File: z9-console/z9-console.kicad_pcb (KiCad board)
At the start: 2 copper layers, 89.5 x 55.5 mm, 130 parts, among them J10 Screw_Terminal_01x06, J2 LCD 3.2" 240x320 Conn_01x14_P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, J4 Conn_01x04_Pin, J6 ST_STDC14 - SAMTEC_FTSH-107-0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, J7 TC2070 - TAG Connect, J801 USB_C_Receptacle_USB2.0_16P, J9 JST GH, Q701 AO3400A, SW2 SW_Push, SW3 SW_Push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

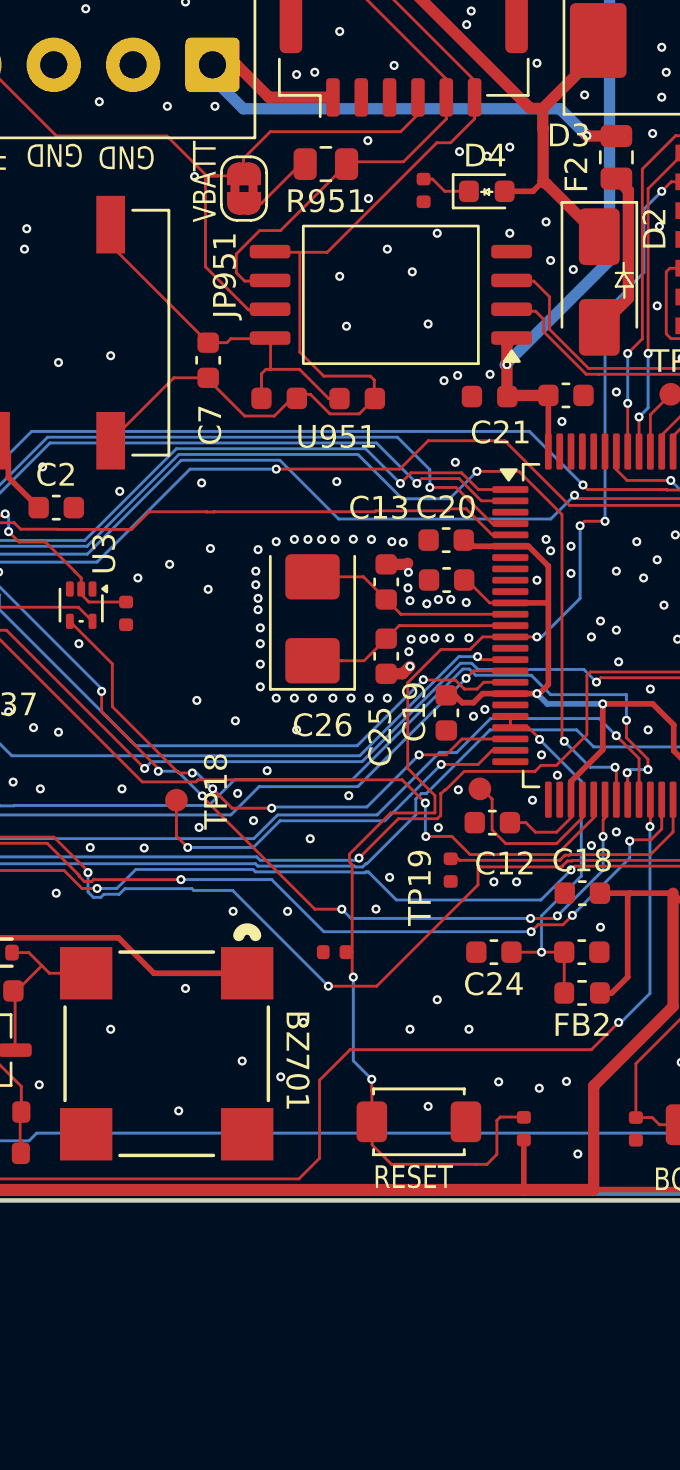
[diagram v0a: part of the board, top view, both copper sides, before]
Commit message: fix 120R resistor up size to match pdm
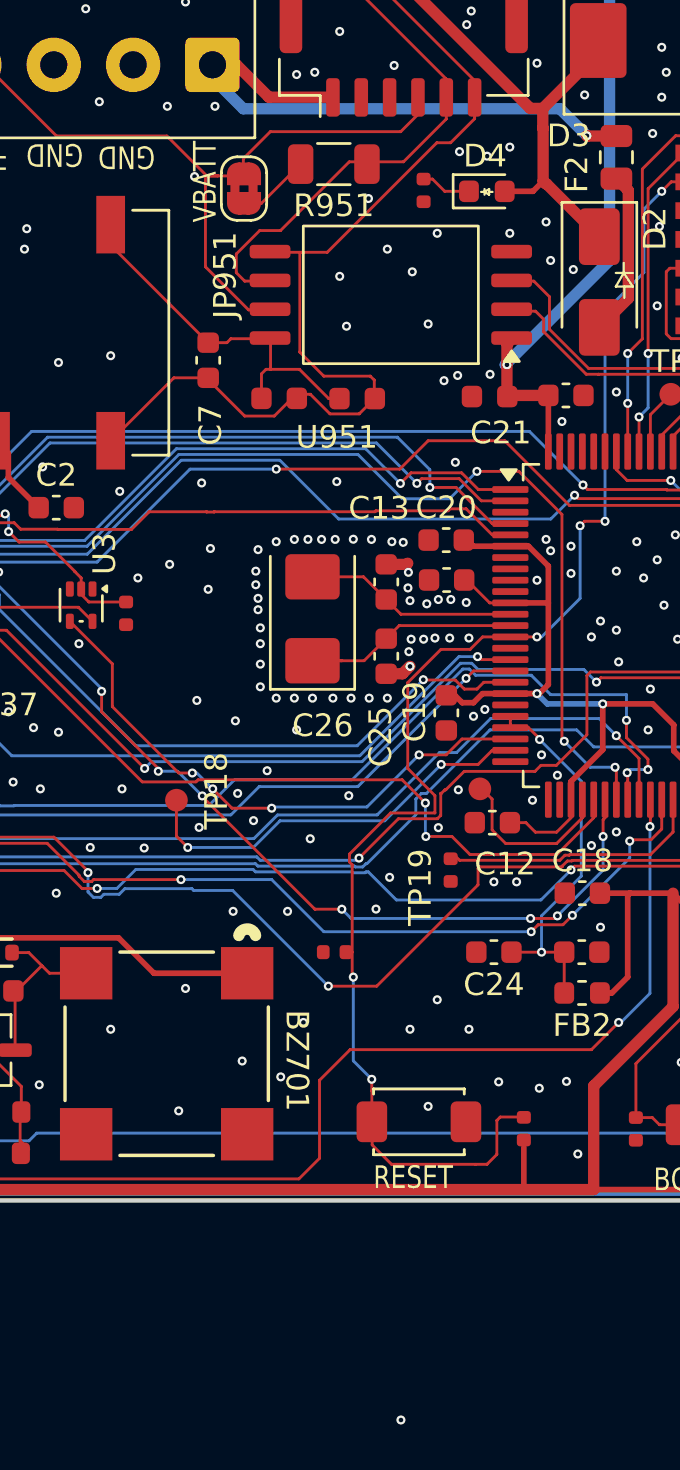
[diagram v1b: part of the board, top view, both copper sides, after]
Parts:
- R951: footprint Resistor_SMD:R_0805_2012Metric -> dnt:R_1206_3216Metric
- moved R951 0.35 mm to (134.0, 81.6)

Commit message: lcsc components and cleanup
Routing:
- net GND: vias 500 -> 505
